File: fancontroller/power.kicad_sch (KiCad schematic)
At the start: 5 parts, among them U3 AMS1117-3.3

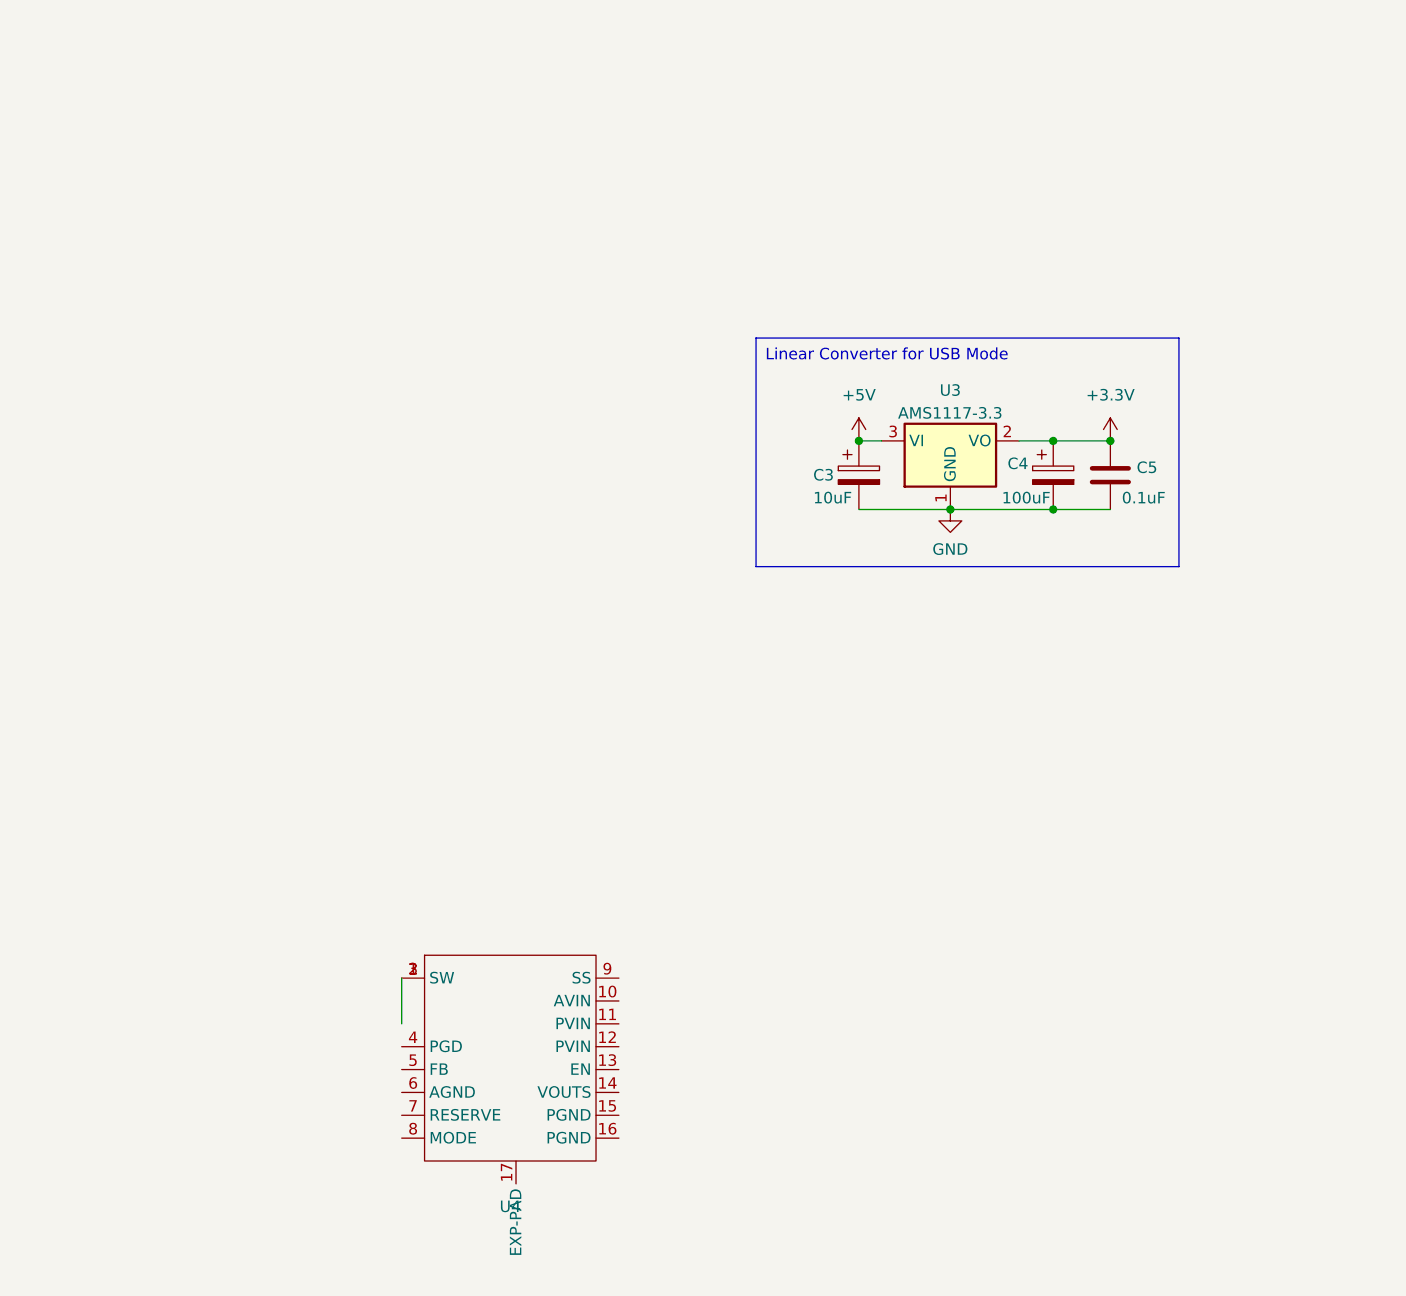
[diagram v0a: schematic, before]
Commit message: Restructure Fan drivers into separate modules and rework USB-C
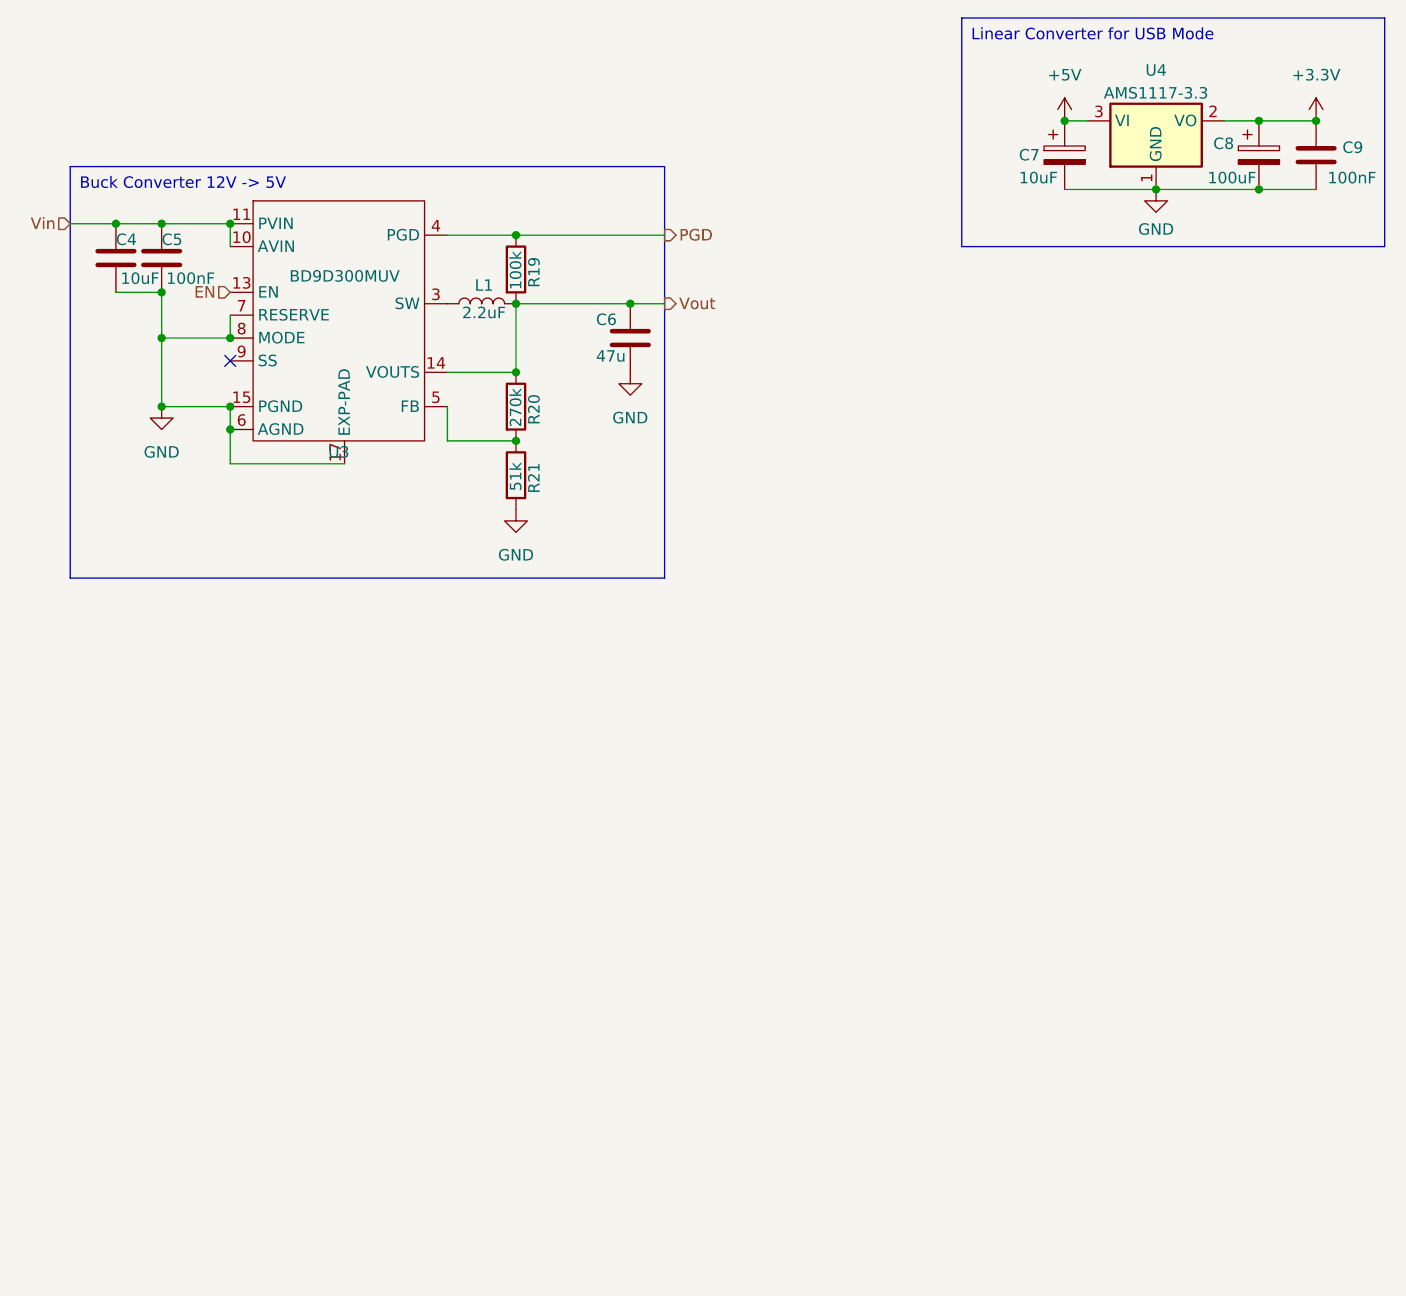
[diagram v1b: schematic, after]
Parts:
- added C4: 10uF, Capacitor_SMD:C_0805_2012Metric, symbol Device:C
- added C5: 100nF, Capacitor_SMD:C_0805_2012Metric, symbol Device:C
- added C6: 47u, symbol Device:C
- added L1: 2.2uF, symbol Device:L
- added R19: 100k, symbol Device:R
- added R20: 270k, symbol Device:R
- added R21: 51k, symbol Device:R
- C9: renamed from C5; value 0.1uF -> 100nF; LCSC Part # C49678 -> C1525
- U3: renamed from U4; value ~ -> BD9D300MUV; LCSC Part # (none) -> C2071880
- U4: renamed from U3; LCSC Part # (none) -> C347256
- renumbered C3 to C7, C4 to C8
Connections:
- net GND: now also U3.15 (PGND), U3.16 (PGND), U3.17 (EXP-PAD), U3.6 (AGND), U3.7 (RESERVE), U3.8 (MODE), C4.2, C5.2, C6.2, R21.2
- net at U3.1 (SW), U3.2 (SW), U3.3 (SW): now also L1.1
- net Vin: now reaches U3.10 (AVIN)
- net Vin: now also U3.11 (PVIN), U3.12 (PVIN), C4.1, C5.1
- net EN: now reaches U3.13 (EN)
- net Vout: now reaches U3.14 (VOUTS)
- net Vout: now also C6.1, L1.2, R19.2, R20.1
- net PGD: now reaches U3.4 (PGD)
- net PGD: now also R19.1
- net at U3.5 (FB): now also R20.2, R21.1
- no-connect marks 0 -> 1
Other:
- company: (none) -> DJ-Bauer
- title: (none) -> Power Circuit
- moved on the sheet: C7, C8, C9, U4

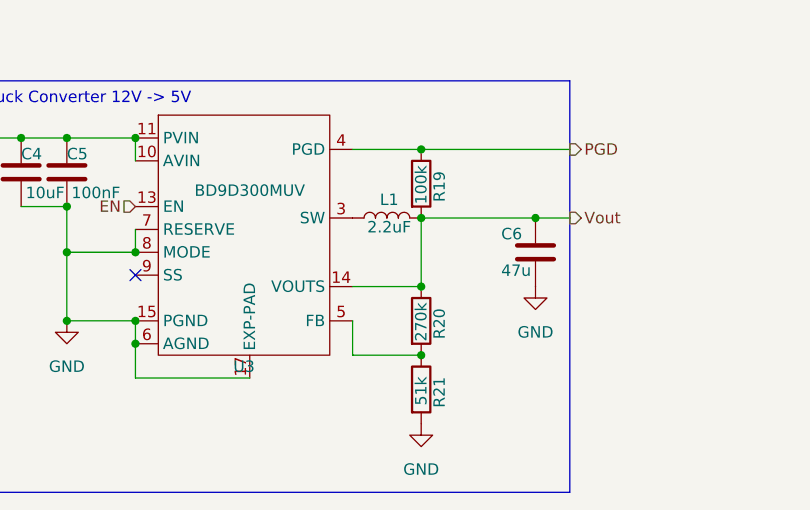
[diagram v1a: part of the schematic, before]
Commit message: Improve footprints and do massive overhaul for part numbering for better future order
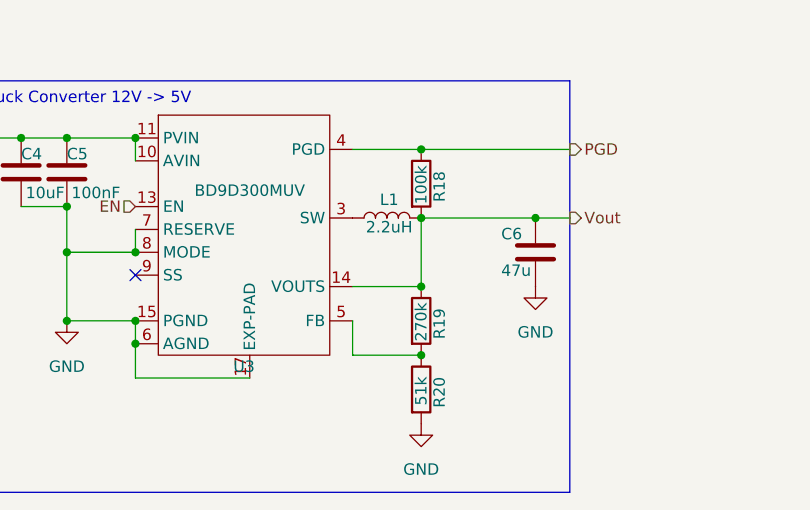
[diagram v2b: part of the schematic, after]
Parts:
- C6: footprint (none) -> Capacitor_SMD:C_0805_2012Metric
- L1: value 2.2uF -> 2.2uH; footprint (none) -> Inductor_SMD:L_0805_2012Metric
- R18: renamed from R19; footprint (none) -> Resistor_SMD:R_0805_2012Metric; LCSC Part # (none) -> C149504
- R19: renamed from R20; footprint (none) -> Resistor_SMD:R_0805_2012Metric; LCSC Part # (none) -> C17589
- R20: renamed from R21; footprint (none) -> Resistor_SMD:R_0805_2012Metric; LCSC Part # (none) -> C17737
- U3: footprint Package_DFN_QFN:VQFN-16-1EP_3x3mm_P0.5mm_EP1.8x1.8mm -> Package_DFN_QFN:VQFN-16-1EP_3x3mm_P0.5mm_EP1.45x1.45mm
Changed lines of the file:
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@@
 			)
 		)
-		(property "Footprint" ""
+		(property "Footprint" "Capacitor_SMD:C_0805_2012Metric"
 			(at 94.9452 71.12 0)
 			(effects
@@
 			)
 		)
+		(property "Power" ""
+			(at 93.98 67.31 0)
+			(effects
+				(font
+					(size 1.27 1.27)
+				)
+				(hide yes)
+			)
+		)
 		(pin "1"
 		)
@@
 			)
 		)
+		(property "Power" ""
+			(at 163.83 46.99 0)
+			(effects
+				(font
+					(size 1.27 1.27)
+				)
+				(hide yes)
+			)
+		)
 		(pin "1"
 		)
@@
 		(on_board yes)
 		(dnp no)
-		(property "Reference" "R20"
+		(property "Reference" "R19"
 			(at 83.312 76.962 90)
 			(effects
@@
 			)
 		)
-		(property "Footprint" ""
+		(property "Footprint" "Resistor_SMD:R_0805_2012Metric"
 			(at 79.502 74.93 90)
 			(effects
@@
 			)
 		)
+		(property "Power" ""
+			(at 81.28 74.93 0)
+			(effects
+				(font
+					(size 1.27 1.27)
+				)
+				(hide yes)
+			)
+		)
+		(property "LCSC Part #" "C17589"
+			(at 81.28 74.93 0)
+			(effects
+				(font
+					(size 1.27 1.27)
+				)
+				(hide yes)
+			)
+		)
 		(pin "1"
 		)
@@
 			(project "fancontroller"
 				(path "/0224fd83-71fd-467a-bea0-55e2843206f4/a9612688-8b33-4507-a26d-2abbbfdabb93"
-					(reference "R20")
+					(reference "R19")
 					(unit 1)
 				)
@@
 		(on_board yes)
 		(dnp no)
-		(property "Reference" "R19"
+		(property "Reference" "R18"
 			(at 83.312 61.722 90)
 			(effects
@@
 			)
 		)
-		(property "Footprint" ""
+		(property "Footprint" "Resistor_SMD:R_0805_2012Metric"
 			(at 79.502 59.69 90)
 			(effects
@@
 			)
 		)
+		(property "Power" ""
+			(at 81.28 59.69 0)
+			(effects
+				(font
+					(size 1.27 1.27)
+				)
+				(hide yes)
+			)
+		)
+		(property "LCSC Part #" "C149504"
+			(at 81.28 59.69 0)
+			(effects
+				(font
+					(size 1.27 1.27)
+				)
+				(hide yes)
+			)
+		)
 		(pin "1"
 		)
@@
 			(project ""
 				(path "/0224fd83-71fd-467a-bea0-55e2843206f4/a9612688-8b33-4507-a26d-2abbbfdabb93"
-					(reference "R19")
+					(reference "R18")
 					(unit 1)
 				)
@@
 			)
 		)
-		(property "Footprint" "Package_DFN_QFN:VQFN-16-1EP_3x3mm_P0.5mm_EP1.8x1.8mm"
+		(property "Footprint" "Package_DFN_QFN:VQFN-16-1EP_3x3mm_P0.5mm_EP1.45x1.45mm"
 			(at 56.642 47.752 0)
 			(effects
@@
 			)
 		)
+		(property "Power" ""
+			(at 55.88 53.34 0)
+			(effects
+				(font
+					(size 1.27 1.27)
+				)
+				(hide yes)
+			)
+		)
 		(pin "4"
 		)
@@
 			)
 		)
+		(property "Power" ""
+			(at 41.91 58.42 0)
+			(effects
+				(font
+					(size 1.27 1.27)
+				)
+				(hide yes)
+			)
+		)
 		(pin "2"
 		)
@@
 		(dnp no)
 		(fields_autoplaced yes)
-		(property "Reference" "#PWR031"
+		(property "Reference" "#PWR033"
 			(at 170.18 46.99 0)
 			(effects
@@
 			(project "fancontroller"
 				(path "/0224fd83-71fd-467a-bea0-55e2843206f4/a9612688-8b33-4507-a26d-2abbbfdabb93"
-					(reference "#PWR031")
+					(reference "#PWR033")
 					(unit 1)
 				)
@@
 		(dnp no)
 		(fields_autoplaced yes)
-		(property "Reference" "#PWR029"
+		(property "Reference" "#PWR031"
 			(at 142.24 46.99 0)
 			(effects
@@
 			(project "fancontroller"
 				(path "/0224fd83-71fd-467a-bea0-55e2843206f4/a9612688-8b33-4507-a26d-2abbbfdabb93"
-					(reference "#PWR029")
+					(reference "#PWR031")
 					(unit 1)
 				)
@@
 			)
 		)
+		(property "Power" ""
+			(at 36.83 58.42 0)
+			(effects
+				(font
+					(size 1.27 1.27)
+				)
+				(hide yes)
+			)
+		)
 		(pin "2"
 		)
@@
 			)
 		)
+		(property "Power" ""
+			(at 170.18 46.99 0)
+			(effects
+				(font
+					(size 1.27 1.27)
+				)
+				(hide yes)
+			)
+		)
 		(pin "1"
 		)
@@
 			)
 		)
-		(property "Value" "2.2uF"
+		(property "Value" "2.2uH"
 			(at 77.724 64.516 90)
 			(effects
@@
 			)
 		)
-		(property "Footprint" ""
+		(property "Footprint" "Inductor_SMD:L_0805_2012Metric"
 			(at 77.47 63.5 0)
 			(effects
@@
 			)
 		)
+		(property "Power" ""
+			(at 77.47 63.5 0)
+			(effects
+				(font
+					(size 1.27 1.27)
+				)
+				(hide yes)
+			)
+		)
 		(pin "2"
 		)
@@
 		(dnp no)
 		(fields_autoplaced yes)
-		(property "Reference" "#PWR026"
+		(property "Reference" "#PWR028"
 			(at 41.91 81.28 0)
 			(effects
@@
 			(project ""
 				(path "/0224fd83-71fd-467a-bea0-55e2843206f4/a9612688-8b33-4507-a26d-2abbbfdabb93"
-					(reference "#PWR026")
+					(reference "#PWR028")
 					(unit 1)
 				)
@@
 			)
 		)
+		(property "Power" ""
+			(at 142.24 46.99 0)
+			(effects
+				(font
+					(size 1.27 1.27)
+				)
+				(hide yes)
+			)
+		)
 		(pin "1"
 		)
@@
 		(dnp no)
 		(fields_autoplaced yes)
-		(property "Reference" "#PWR027"
+		(property "Reference" "#PWR029"
 			(at 81.28 92.71 0)
 			(effects
@@
 			(project "fancontroller"
 				(path "/0224fd83-71fd-467a-bea0-55e2843206f4/a9612688-8b33-4507-a26d-2abbbfdabb93"
-					(reference "#PWR027")
+					(reference "#PWR029")
 					(unit 1)
 				)
@@
 		(on_board yes)
 		(dnp no)
-		(property "Reference" "R21"
+		(property "Reference" "R20"
 			(at 83.312 84.582 90)
 			(effects
@@
 			)
 		)
-		(property "Footprint" ""
+		(property "Footprint" "Resistor_SMD:R_0805_2012Metric"
 			(at 79.502 82.55 90)
 			(effects
@@
 			)
 		)
+		(property "Power" ""
+			(at 81.28 82.55 0)
+			(effects
+				(font
+					(size 1.27 1.27)
+				)
+				(hide yes)
+			)
+		)
+		(property "LCSC Part #" "C17737"
+			(at 81.28 82.55 0)
+			(effects
+				(font
+					(size 1.27 1.27)
+				)
+				(hide yes)
+			)
+		)
 		(pin "1"
 		)
@@
 			(project "fancontroller"
 				(path "/0224fd83-71fd-467a-bea0-55e2843206f4/a9612688-8b33-4507-a26d-2abbbfdabb93"
-					(reference "R21")
+					(reference "R20")
 					(unit 1)
 				)
@@
 		(dnp no)
 		(fields_autoplaced yes)
-		(property "Reference" "#PWR030"
+		(property "Reference" "#PWR032"
 			(at 152.4 57.15 0)
 			(effects
@@
 			(project "fancontroller"
 				(path "/0224fd83-71fd-467a-bea0-55e2843206f4/a9612688-8b33-4507-a26d-2abbbfdabb93"
-					(reference "#PWR030")
+					(reference "#PWR032")
 					(unit 1)
 				)
@@
 			)
 		)
+		(property "Power" ""
+			(at 152.4 43.18 0)
+			(effects
+				(font
+					(size 1.27 1.27)
+				)
+				(hide yes)
+			)
+		)
 		(pin "1"
 		)
@@
 		(dnp no)
 		(fields_autoplaced yes)
-		(property "Reference" "#PWR028"
+		(property "Reference" "#PWR030"
 			(at 93.98 77.47 0)
 			(effects
@@
 			(project ""
 				(path "/0224fd83-71fd-467a-bea0-55e2843206f4/a9612688-8b33-4507-a26d-2abbbfdabb93"
-					(reference "#PWR028")
-					(unit 1)
-				)
+					(reference "#PWR030")
+					(unit 1)
+				)

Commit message: edit schematic
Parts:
- U3: footprint Package_DFN_QFN:VQFN-16-1EP_3x3mm_P0.5mm_EP1.45x1.45mm -> DJCustom:VQFN-16-1EP_3x3mm_P0.5mm_EP1.45x1.45mm
- U4: footprint Package_TO_SOT_SMD:SOT-223-3_TabPin2 -> Package_TO_SOT_SMD:SOT-223; LCSC Part # C347256 -> C6186
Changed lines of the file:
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@@
 			)
 		)
-		(property "Footprint" "Package_DFN_QFN:VQFN-16-1EP_3x3mm_P0.5mm_EP1.45x1.45mm"
+		(property "Footprint" "DJCustom:VQFN-16-1EP_3x3mm_P0.5mm_EP1.45x1.45mm"
 			(at 56.642 47.752 0)
 			(effects
@@
 			)
 		)
-		(property "Footprint" "Package_TO_SOT_SMD:SOT-223-3_TabPin2"
+		(property "Footprint" "Package_TO_SOT_SMD:SOT-223"
 			(at 152.4 38.1 0)
 			(effects
@@
 			)
 		)
-		(property "LCSC Part #" "C347256"
+		(property "LCSC Part #" "C6186"
 			(at 152.4 43.18 0)
 			(effects
